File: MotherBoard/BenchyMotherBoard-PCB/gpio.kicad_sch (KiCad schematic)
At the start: 39 parts, among them J2 SWD-TAG, J3 FILES-SD-CARD, J7 BOOT-SD-CARD, J8 FAN-CONN, Q1 SQ2310ES_SOT23, Q2 MMBT2222A, SW1 BOOT-SEL, U1 STM32MP157FAB1, Y1 24MHz, Y2 32.7KHz

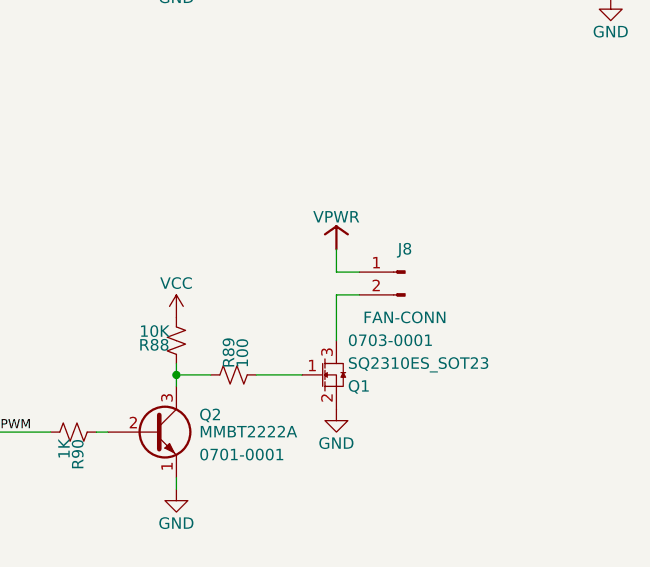
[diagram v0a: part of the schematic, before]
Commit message: Initial DDR routing, start fixing skew
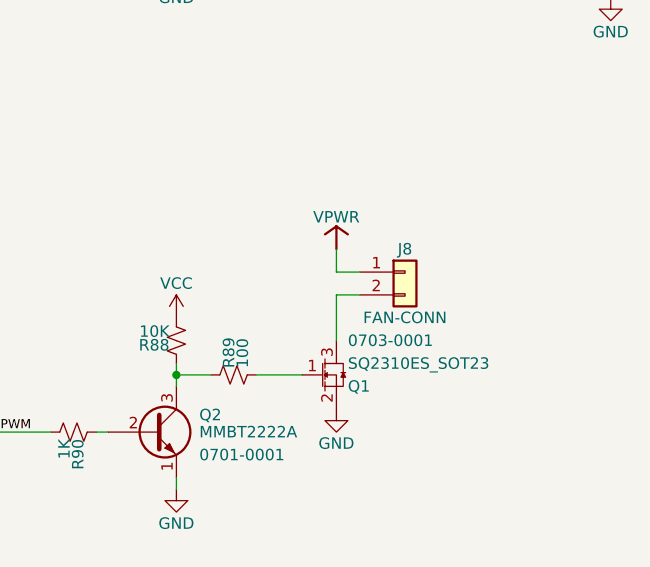
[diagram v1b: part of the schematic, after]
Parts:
- removed J8: FAN-CONN, Connector_PinHeader_2.54mm:PinHeader_1x02_P2.54mm_Vertical, symbol Connector:Conn_01x02_Male
- added J8: FAN-CONN, Connector_PinHeader_2.54mm:PinHeader_1x02_P2.54mm_Vertical, symbol Connector_Generic:Conn_01x02
- U1: footprint Daxxn_Packages:LFBGA354-P0.8mm -> Daxxn_Packages:LFBGA354-P0.8mm-STM32MP157F
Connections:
- net VPWR: now also J8.1 (Pin_1)
- net at Q1.3 (D): now also J8.2 (Pin_2)
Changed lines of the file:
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@@
       (effects (font (size 1.27 1.27)) (justify left))
     )
-    (property "Footprint" "Daxxn_Packages:LFBGA354-P0.8mm" (at 128.27 90.17 0)
+    (property "Footprint" "Daxxn_Packages:LFBGA354-P0.8mm-STM32MP157F" (at 128.27 90.17 0)
       (effects (font (size 1.27 1.27)) (justify left) hide)
     )
@@
       (effects (font (size 1.27 1.27)) (justify left))
     )
-    (property "Footprint" "Daxxn_Packages:LFBGA354-P0.8mm" (at 128.27 207.01 0)
+    (property "Footprint" "Daxxn_Packages:LFBGA354-P0.8mm-STM32MP157F" (at 128.27 207.01 0)
       (effects (font (size 1.27 1.27)) (justify left) hide)
     )
@@
     )
   )
-  (symbol (lib_id "Connector:Conn_01x02_Male") (at 539.75 162.56 0) (mirror y) (unit 1)
-    (in_bom yes) (on_board yes) (dnp no)
-    (property "Reference" "J8" (at 539.75 160.02 0)
-      (effects (font (size 1.27 1.27)))
-    )
-    (property "Value" "FAN-CONN" (at 539.75 167.64 0)
-      (effects (font (size 1.27 1.27)))
-    )
-    (property "Footprint" "Connector_PinHeader_2.54mm:PinHeader_1x02_P2.54mm_Vertical" (at 539.75 162.56 0)
-      (effects (font (size 1.27 1.27)) hide)
-    )
-    (property "Datasheet" "~" (at 539.75 162.56 0)
-      (effects (font (size 1.27 1.27)) hide)
-    )
-    (pin "1")
-    (pin "2")
-    (instances
-      (project "BenchyMotherBoard-PCB"
-        (path "/2ea077fe-b0e6-467f-a1c1-8336ebdb7a86/76adaf3c-f4c9-4828-81af-280c66ff42c8"
-          (reference "J8") (unit 1)
-        )
-      )
-    )
-  )
   (symbol (lib_id "power:VDD") (at 514.35 88.9 0) (unit 1)
     (in_bom yes) (on_board yes) (dnp no)
@@
     )
   )
+  (symbol (lib_id "Connector_Generic:Conn_01x02") (at 539.75 162.56 0) (unit 1)
+    (in_bom yes) (on_board yes) (dnp no)
+    (property "Reference" "J8" (at 539.75 160.02 0)
+      (effects (font (size 1.27 1.27)))
+    )
+    (property "Value" "FAN-CONN" (at 539.75 167.64 0)
+      (effects (font (size 1.27 1.27)))
+    )
+    (property "Footprint" "Connector_PinHeader_2.54mm:PinHeader_1x02_P2.54mm_Vertical" (at 539.75 162.56 0)
+      (effects (font (size 1.27 1.27)) hide)
+    )
+    (property "Datasheet" "~" (at 539.75 162.56 0)
+      (effects (font (size 1.27 1.27)) hide)
+    )
+    (property "Schematic" "" (at 539.75 162.56 0)
+      (effects (font (size 1.27 1.27)) hide)
+    )
+    (property "PartNumber" "" (at 539.75 162.56 0)
+      (effects (font (size 1.27 1.27)))
+    )
+    (property "SupplierPN" "" (at 539.75 162.56 0)
+      (effects (font (size 1.27 1.27)) hide)
+    )
+    (pin "1")
+    (pin "2")
+    (instances
+      (project "BenchyMotherBoard-PCB"
+        (path "/2ea077fe-b0e6-467f-a1c1-8336ebdb7a86/76adaf3c-f4c9-4828-81af-280c66ff42c8"
+          (reference "J8") (unit 1)
+        )
+      )
+    )
+  )
   (symbol (lib_id "Device:C_Small") (at 186.69 77.47 0) (mirror x) (unit 1)
     (in_bom yes) (on_board yes) (dnp no)
@@
       (effects (font (size 1.27 1.27)) (justify left))
     )
-    (property "Footprint" "Daxxn_Packages:LFBGA354-P0.8mm" (at 127 44.45 0)
+    (property "Footprint" "Daxxn_Packages:LFBGA354-P0.8mm-STM32MP157F" (at 127 44.45 0)
       (effects (font (size 1.27 1.27)) (justify left) hide)
     )
@@
       (effects (font (size 1.27 1.27)) (justify left))
     )
-    (property "Footprint" "Daxxn_Packages:LFBGA354-P0.8mm" (at 128.27 148.59 0)
+    (property "Footprint" "Daxxn_Packages:LFBGA354-P0.8mm-STM32MP157F" (at 128.27 148.59 0)
       (effects (font (size 1.27 1.27)) (justify left) hide)
     )

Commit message: REV1 - Finish layout and finalize pcb
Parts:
- added D16 (x4): RED, LED_SMD:LED_0805_2012Metric, symbol Device:LED_Small
- added R120 (x4): 500, Resistor_SMD:R_0402_1005Metric, symbol Device:R_Small_US
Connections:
- net GND: now also R120.2, R120.2, R120.2, R120.2
- net WARNING-IND: now reaches U1.D9 (PB9)
- net WARNING-IND: now also D16.2 (A)
- net USB-STATUS: now reaches U1.A9 (PC7)
- net USB-STATUS: now also D16.2 (A)
- net GLOBAL-STATUS: now reaches U1.B10 (PD2)
- net GLOBAL-STATUS: now also D16.2 (A)
- net DISPLAY-STATUS: now reaches U1.C10 (PC12)
- net DISPLAY-STATUS: now also D16.2 (A)
- new net: D16.1 (K), R120.1 (x4)

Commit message: Add volt meter PCB
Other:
- note added: "BOOT SD-CARD"
- note added: "BUS BREAKOUT"
- note added: "FAN CONTROL"
- note added: "STATUS IND"
- note added: "STM32 MPU CTRL"
- note added: "STM32 MPU GPIO"
- note added: "STORAGE SD-CARD"
- note added: "SWD"
- moved on the sheet: C137, C138, C139, C140, C141, C142, C143, C144, D16, J2, J3, J7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

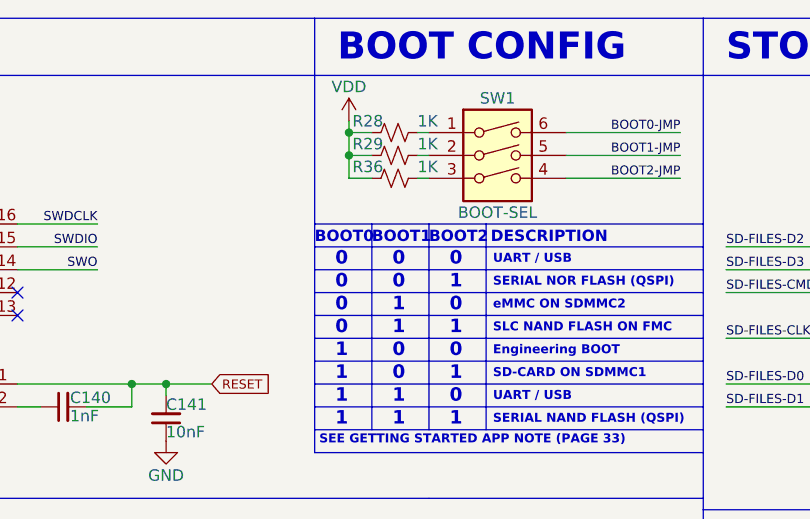
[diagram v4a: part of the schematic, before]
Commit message: Wrap up REV2 and add voltmeter gerbers
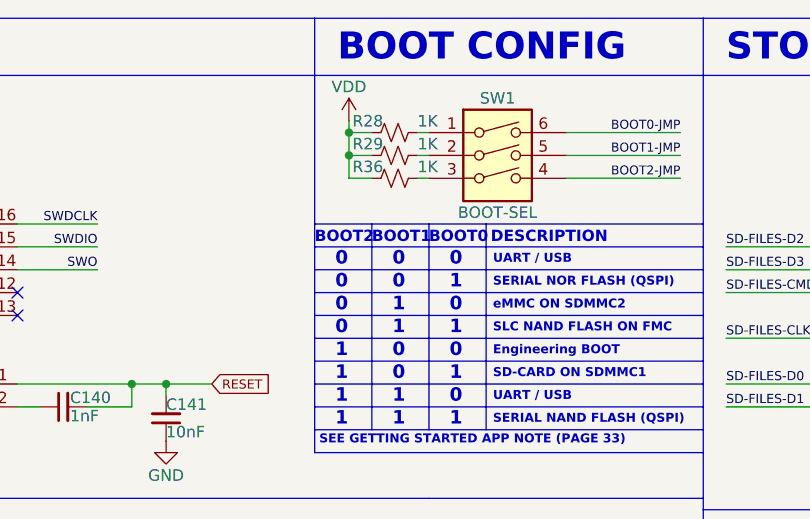
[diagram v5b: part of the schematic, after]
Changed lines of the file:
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@@
     (effects (font (size 1 1) (thickness 0.2032) bold) (justify left bottom))
   )
-  (text "BOOT0" (at 203.2 37.846 0)
+  (text "BOOT2" (at 203.2 37.846 0)
     (effects (font (size 1.25 1.25) (thickness 0.2032) bold) (justify left bottom))
   )
@@
     (effects (font (size 1.5 1.5) (thickness 0.2032) bold) (justify left bottom))
   )
-  (text "BOOT2" (at 215.9 37.846 0)
+  (text "BOOT0" (at 215.9 37.846 0)
     (effects (font (size 1.25 1.25) (thickness 0.2032) bold) (justify left bottom))
   )

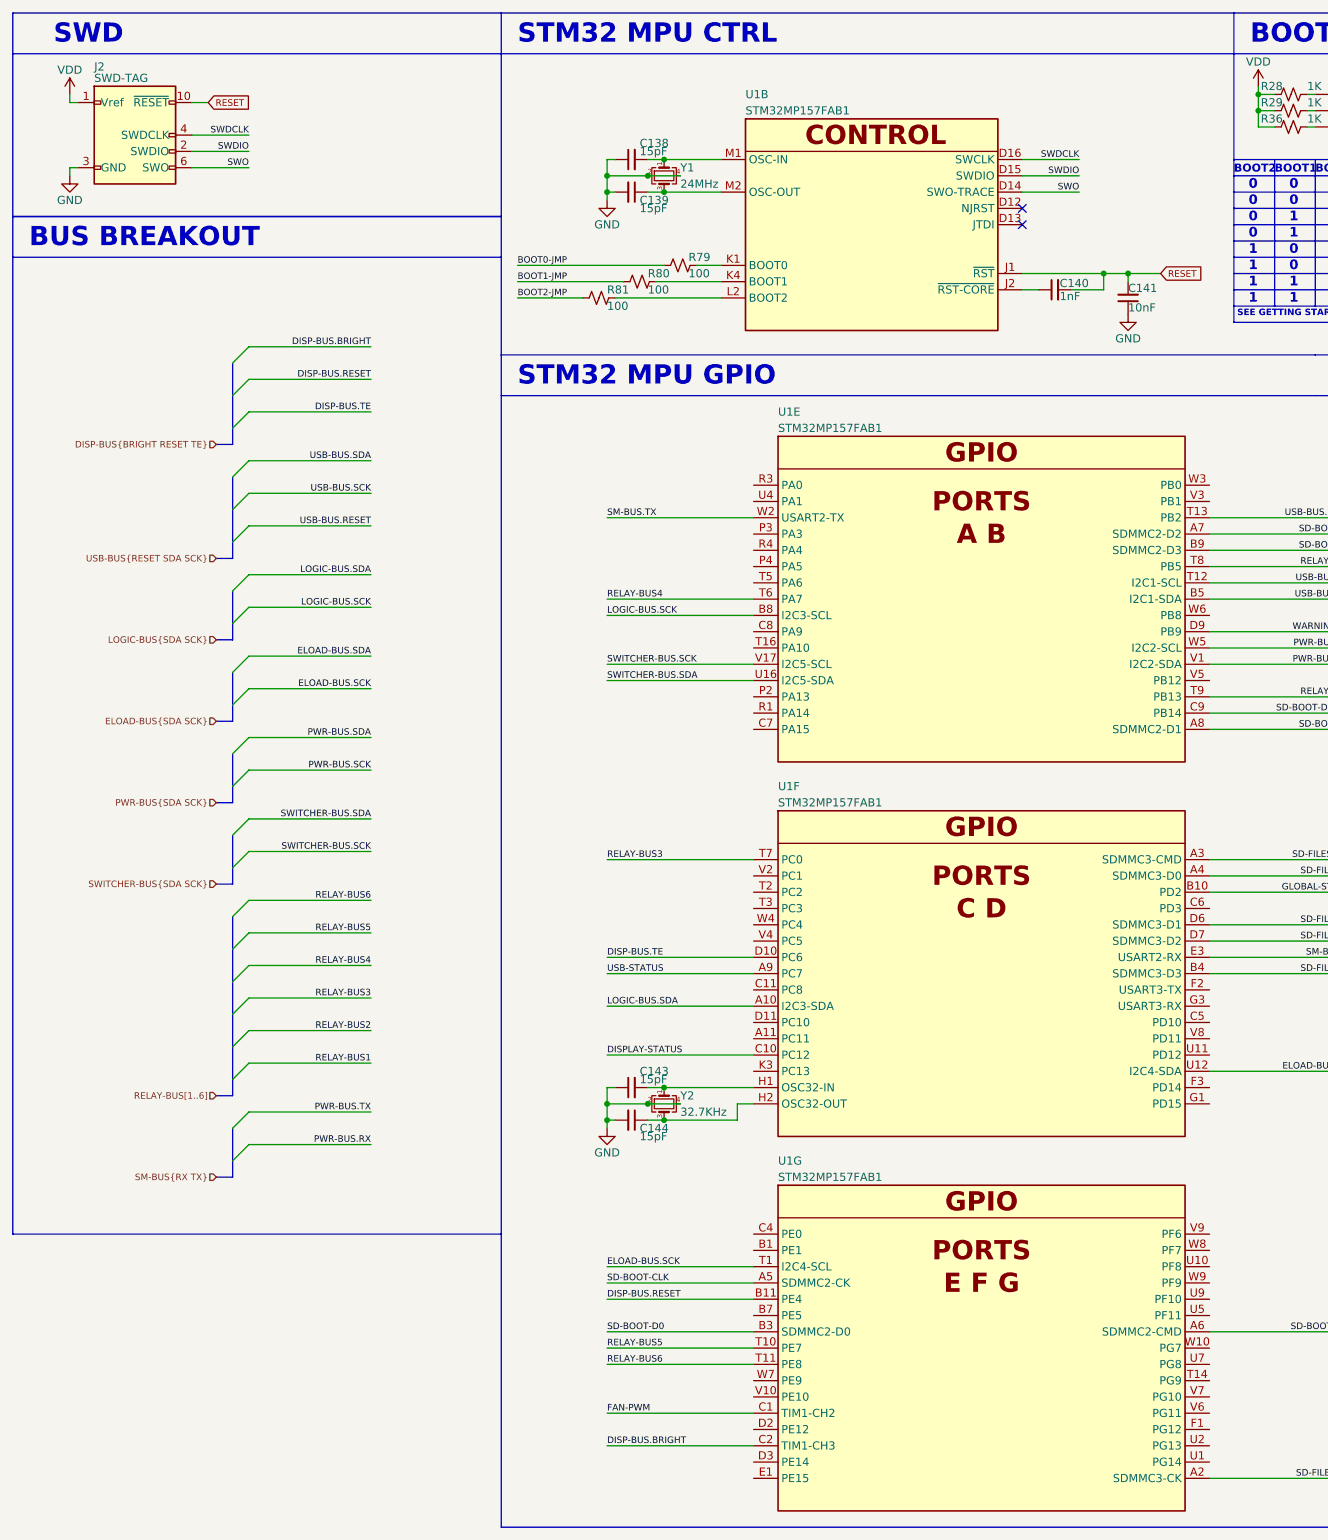
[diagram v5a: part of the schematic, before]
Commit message: (!!WIP!!) Started schematic and block diagram
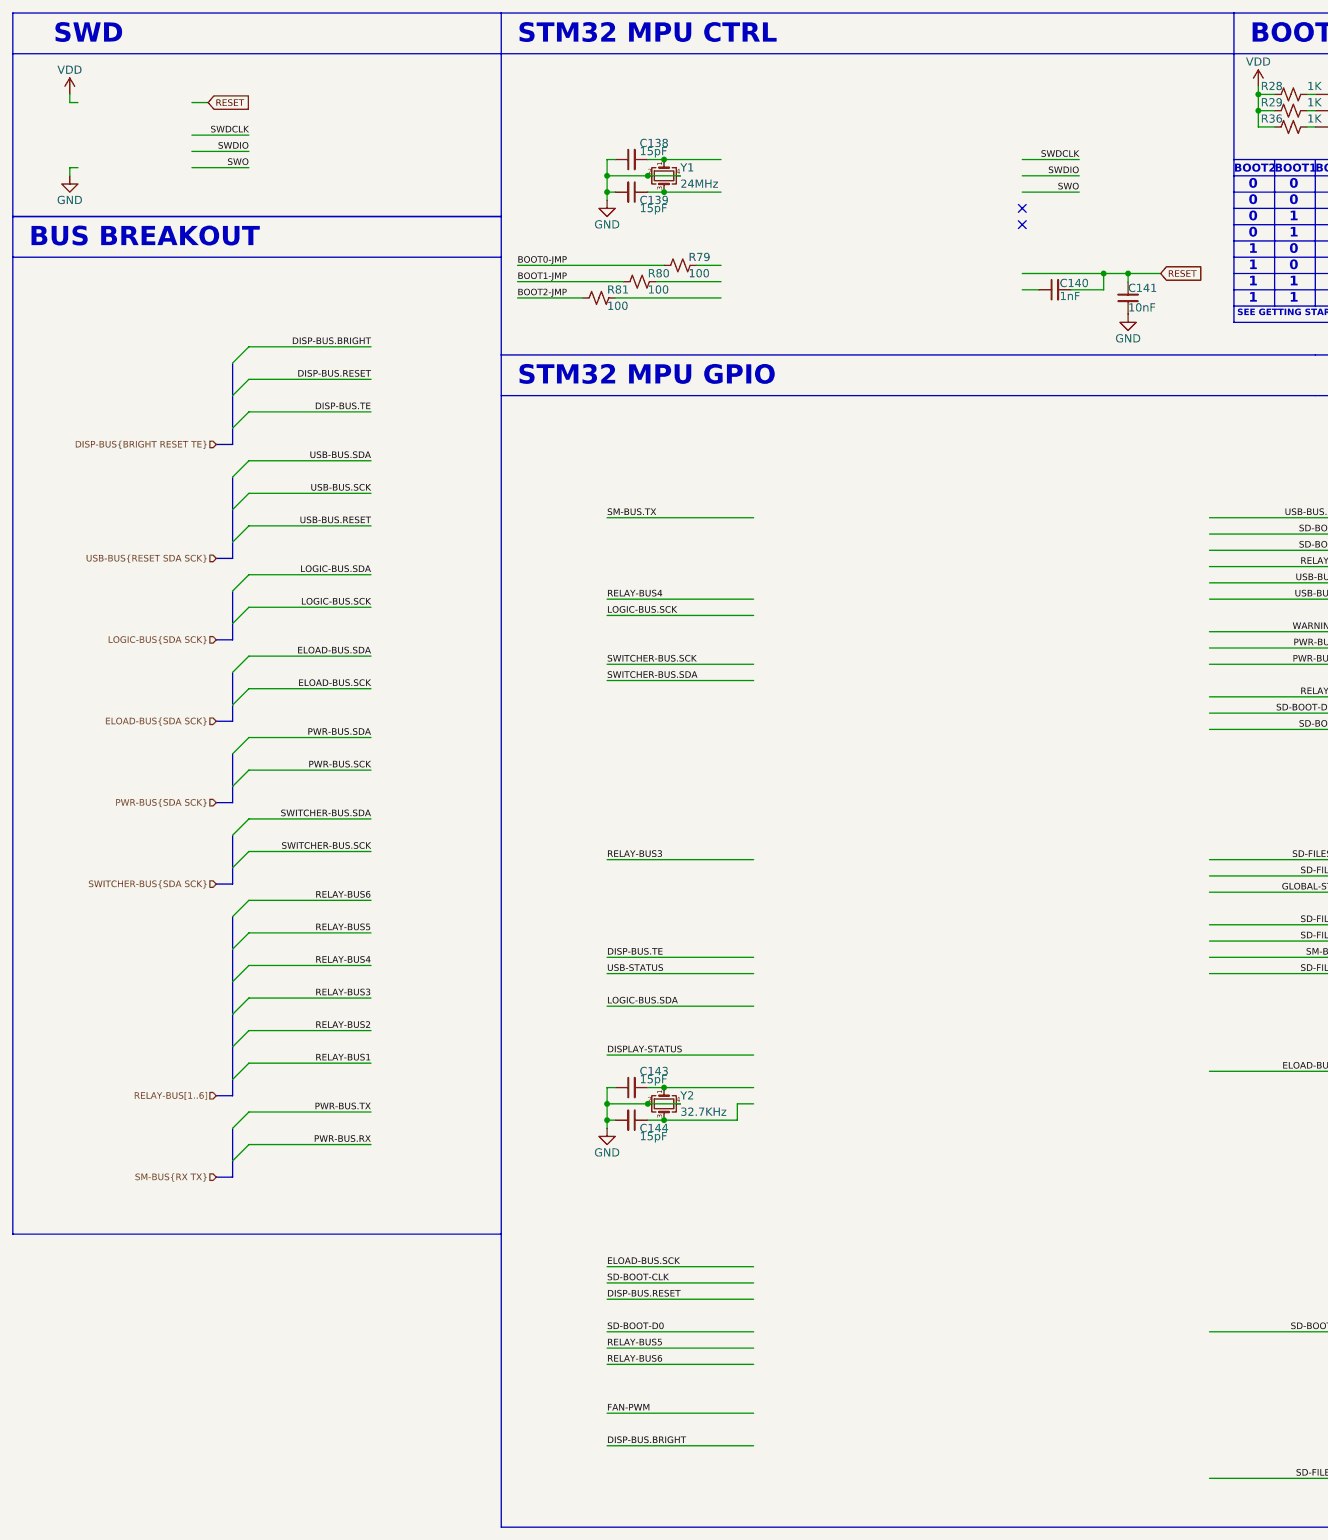
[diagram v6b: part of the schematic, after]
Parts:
- removed J2: SWD-TAG, Connector:Tag-Connect_TC2050-IDC-FP_2x05_P1.27mm_Vertical, symbol Daxxn_Connectors:SWD-TAG
- removed U1: STM32MP157FAB1, Daxxn_Packages:LFBGA354-P0.8mm-STM32MP157F, symbol Daxxn_MicroProcessors:STM32MP157FAB1

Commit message: (WIP) Finish more of the PS schematic
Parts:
- added U4: AM6254ATCGGAALW, Daxxn_Packages:ALW0425A-BGA-425-13x13mm, symbol Daxxn_TIMicros:AM6254ATCGGAALW

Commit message: (WIP) Complete most of the PS and boot schematics
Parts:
- removed C137, C142: 4.7uF, Capacitor_SMD:C_0805_2012Metric, symbol Device:C_Small
- removed C143, C144: 15pF, Capacitor_SMD:C_0402_1005Metric, symbol Device:C_Small
- removed D16 (x4): RED, LED_SMD:LED_0805_2012Metric, symbol Device:LED_Small
- removed J3: FILES-SD-CARD, Daxxn_Connectors:microSD_HC_Molex_47219-2001, symbol Connector:Micro_SD_Card
- removed J7: BOOT-SD-CARD, Daxxn_Connectors:microSD_HC_Molex_47219-2001, symbol Connector:Micro_SD_Card
- removed R120 (x4): 500, Resistor_SMD:R_0402_1005Metric, symbol Device:R_Small_US
- removed R73, R82: 10K, Resistor_SMD:R_0402_1005Metric, symbol Device:R_Small_US
- removed R74, R75, R76, R77, R78, R83, R84, R85, R86, R87: 47K, Resistor_SMD:R_0402_1005Metric, symbol Device:R_Small_US
- removed unit 12 of U4
- removed unit 3 of U4
- removed unit 2 of U4
- removed Y2: 32.7KHz, Daxxn_Passives:Crystal_SMD_4Pin_3.2x2.5mm, symbol Device:Crystal_GND24_Small
- added C97, C98: 100nF, Capacitor_SMD:C_0201_0603Metric, symbol Daxxn_Device:C
- added R128, R129: 10K, Resistor_SMD:R_0201_0603Metric, symbol Daxxn_Device:R
- added R130, R131, R132, R133: 4.7K, Resistor_SMD:R_0402_1005Metric, symbol Daxxn_Device:R
- added U27, U28: TMP100NA, Daxxn_Packages:SOT-23-6, symbol Daxxn_Sensors:TMP100NA
- C138, C139, C140, C141: symbol Device:C_Small -> Daxxn_Device:C
- R28, R29, R36, R79, R80, R81, R88, R89, R90: symbol Device:R_Small_US -> Daxxn_Device:R
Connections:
- net GND: now also C97.2, C98.2, U27.2 (GND), U28.2 (GND), U28.5 (ADD0)
- net VDD: now also C97.1, C98.1, R128.1, R129.1, R130.1, R131.1, R132.1, R133.1, U27.4 (VCC), U27.5 (ADD0), U28.4 (VCC)
- net I2C-SYS-SDA: now reaches U4.A16 (I2C0-SDA)
- net I2C-SYS-SDA: now also R130.2, U27.6 (SDA), U28.6 (SDA)
- net I2C-MAIN-SDA: now reaches U4.A17 (I2C1-SDA)
- net I2C-MAIN-SDA: now also R133.2
- net I2C-SYS-SCL: now reaches U4.B16 (I2C0-SCL)
- net I2C-SYS-SCL: now also R131.2, U27.1 (SCL), U28.1 (SCL)
- net I2C-MAIN-SCL: now reaches U4.B17 (I2C1-SCL)
- net I2C-MAIN-SCL: now also R132.2
- net CAN-RX: now reaches U4.C15 (MCAN0-TX)
- net CAN-TX: now reaches U4.E15 (MCAN0-RX)
- new net TEMP-ALERT: R128.2, R129.2, U27.3 (~{ALERT}), U28.3 (~{ALERT})
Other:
- note added: "TEMP SENSORS"
- note removed: "BOOT SD-CARD"
- note removed: "BUS BREAKOUT"
- note removed: "STATUS IND"
- note removed: "STM32 MPU CTRL"
- note removed: "STM32 MPU GPIO"
- note removed: "STORAGE SD-CARD"
- note removed: "SWD"
- moved on the sheet: C138, C139, C140, C141, R28, R29, R36, R79, R80, R81, SW1, U4J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
